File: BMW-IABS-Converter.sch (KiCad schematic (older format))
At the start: 43 parts, among them J1 SWD, J2 BMW_MOTORRAD, Q1 IRLML0060TRPbF, Q2 IRLML0060TRPbF, Q3 IRFR9024, Q4 IRFR9024, U1 LM358, U2 LM358, U3 LM358, U4 LM358

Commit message: Updated schematics
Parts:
- removed Q4: IRFR9024, Package_TO_SOT_SMD:TO-252-2, symbol Device:Q_PMOS_GDS
- removed R15: 10K, Resistor_SMD:R_0402_1005Metric, symbol Device:R
- removed U4: LM358, Package_SO:SOIC-8_3.9x4.9mm_P1.27mm, symbol Amplifier_Operational:LM358
- added Q6: IRFR9024, Package_TO_SOT_SMD:TO-252-2, symbol Device:Q_PMOS_GDS
- added R13: 200R, Capacitor_SMD:C_0402_1005Metric, symbol Device:R
- added U4: LM2904, symbol Amplifier_Operational:LM2904
- C11: value 1uF -> 10uF
- R11: value 10R -> 1K; footprint Resistor_SMD:R_0402_1005Metric -> (none)
- R12: value 10K -> 1K; footprint Resistor_SMD:R_0402_1005Metric -> (none)
- R14: value 10R -> 200R; footprint Resistor_SMD:R_0402_1005Metric -> Capacitor_SMD:C_0402_1005Metric
- R17: renamed from R13; value 1K -> 100R
- U1: value LM358 -> SN65HVD230
- U2: value LM358 -> STM32F042F4P6
- U3: value LM358 -> MC34063AD
- renumbered Q3 to Q4
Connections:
- net SPEED is gone; now on net SPEED_PWM: U2.13 (PA7)
- net +12V: now also Q4.3 (S), Q6.3 (S), U4.8 (V+); no longer Q4.2 (D)
- net +3V3: now also R11.1; no longer R12.1
- net 54: now also Q6.2 (D)
- net 58RL: now also Q4.2 (D); no longer Q4.3 (S)
- net BRAKE_LIGHT: now also U2.9 (PA3), U4.5 (+); no longer R14.2
- net GND: now also R12.2, U4.4 (V-)
- net SPEED_PWM: now also U2.8 (PA2)
- net TAIL_LIGHT: now also U2.10 (PA4), U4.3 (+); no longer R11.2
- net TAS: now also C11.1, R17.1
- net at R14.1: now also Q6.1 (G)
- new net: R13.2, U4.1
- new net: R14.2, U4.7
- new net: Q4.1 (G), R13.1
- new net 1V6: R11.2, R12.1, U4.2 (-), U4.6 (-)
- no-connect marks 10 -> 7
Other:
- moved on the sheet: C11, D4, Q4, R17

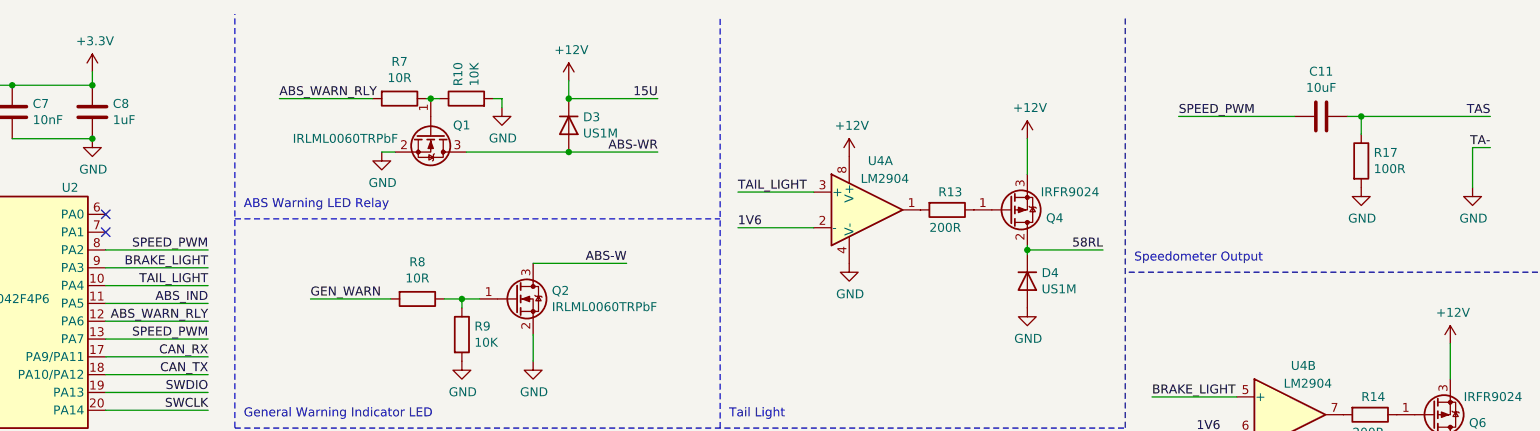
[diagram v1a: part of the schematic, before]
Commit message: Fixed schematics
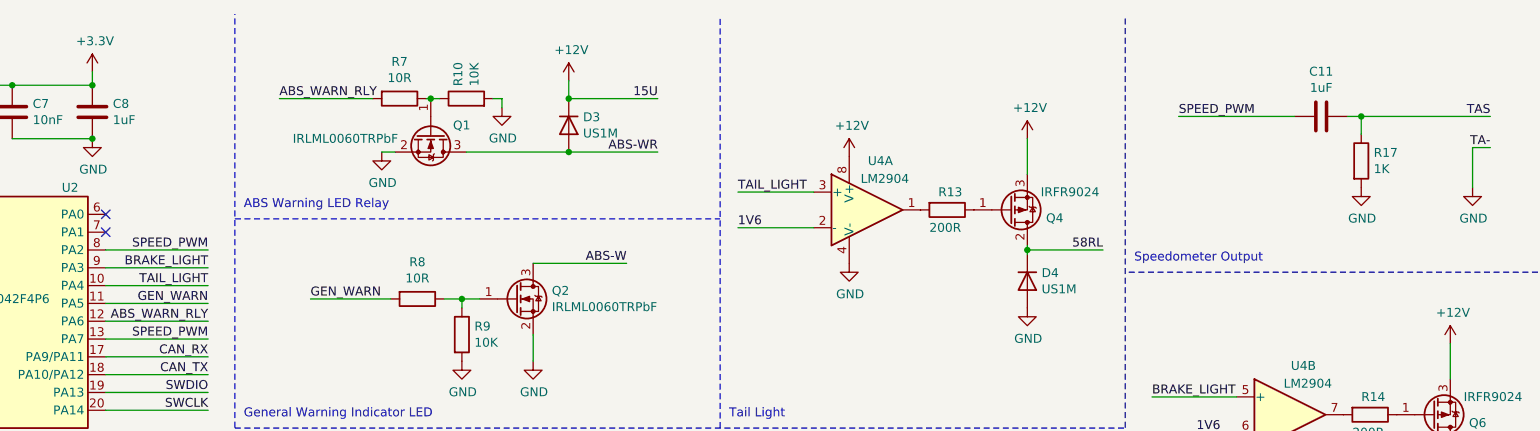
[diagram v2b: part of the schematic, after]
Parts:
- C11: value 10uF -> 1uF
- R17: value 100R -> 1K
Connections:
- net ABS_IND is gone; now on net GEN_WARN: U2.11 (PA5)
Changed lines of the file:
@@
 Text Notes 3850 2725 0    50   ~ 0
 General Warning Indicator LED
-Text Label 3650 2075 2    50   ~ 0
-ABS_IND
 Wire Wire Line
 	3650 2075 3075 2075
@@
 P 9900 1025
 F 0 "C11" V 9648 1025 50  0000 C CNN
-F 1 "10uF" V 9739 1025 50  0000 C CNN
+F 1 "1uF" V 9739 1025 50  0000 C CNN
 F 2 "Capacitor_SMD:C_0603_1608Metric" H 9938 875 50  0001 C CNN
 F 3 "~" H 9900 1025 50  0001 C CNN
@@
 P 10125 1275
 F 0 "R17" H 10195 1321 50  0000 L CNN
-F 1 "100R" H 10195 1230 50  0000 L CNN
+F 1 "1K" H 10195 1230 50  0000 L CNN
 F 2 "Capacitor_SMD:C_0402_1005Metric" V 10055 1275 50  0001 C CNN
 F 3 "~" H 10125 1275 50  0001 C CNN
@@
 	0    1    1    0
 $EndComp
+Text Label 3650 2075 2    50   ~ 0
+GEN_WARN
 $EndSCHEMATC
